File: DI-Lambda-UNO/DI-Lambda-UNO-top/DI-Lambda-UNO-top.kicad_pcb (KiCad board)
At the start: 2 copper layers, 38.2 x 125 mm, 13 parts, among them J1 CONN_02X04, J10 CONN_02X04, J11 CONN_02X04, J12 CONN_02X04, J2 CONN_02X04, J3 CONN_02X04, J4 CONN_02X04, J5 CONN_02X04, J6 CONN_02X04, J7 CONN_02X04, J8 CONN_02X04, J9 CONN_02X04

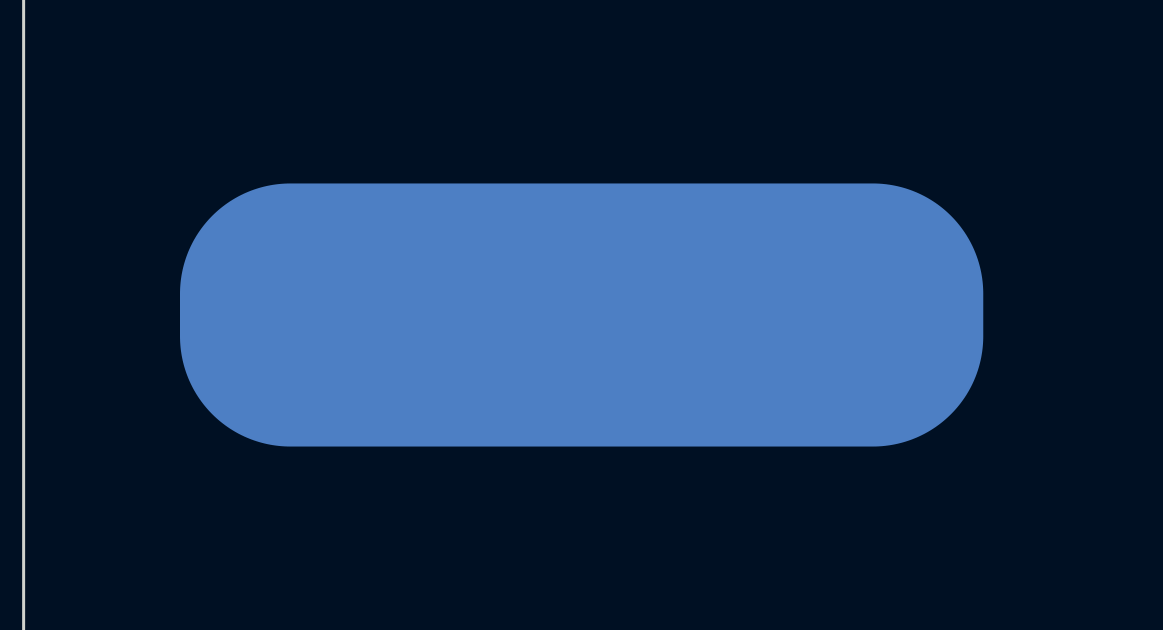
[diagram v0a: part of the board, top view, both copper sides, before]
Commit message: DI-Lambda UNO top panel cleanup
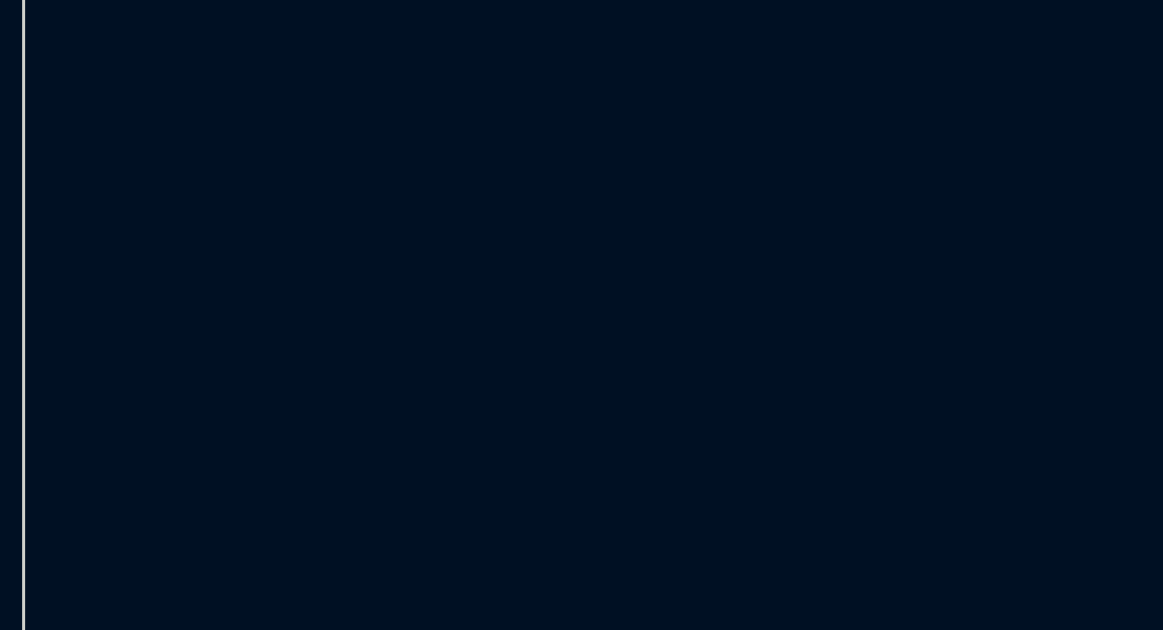
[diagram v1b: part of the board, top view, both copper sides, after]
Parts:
- removed svg2mod: G***, svg2mod:DI-Lambda-UNO-for-Kicad-top-mask

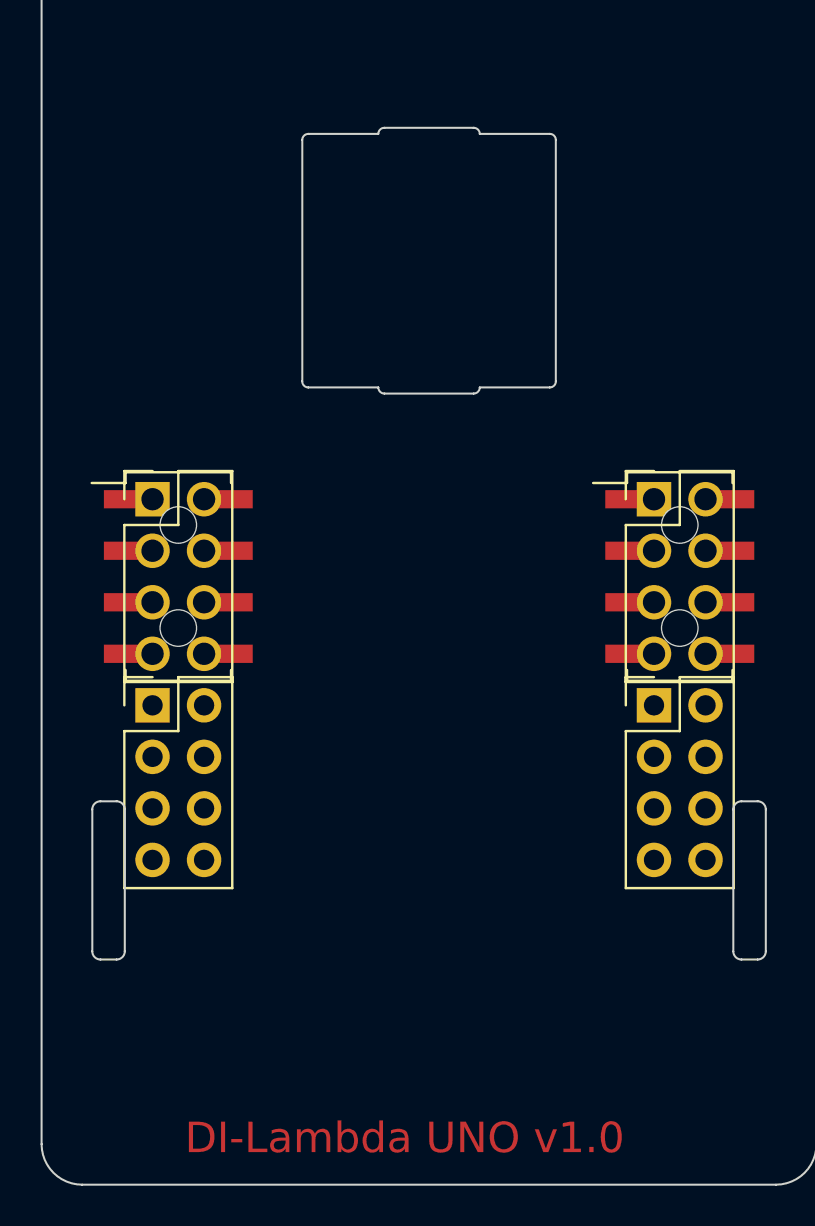
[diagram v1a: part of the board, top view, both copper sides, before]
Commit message: Increase top plate cuvette hole size to 13mm
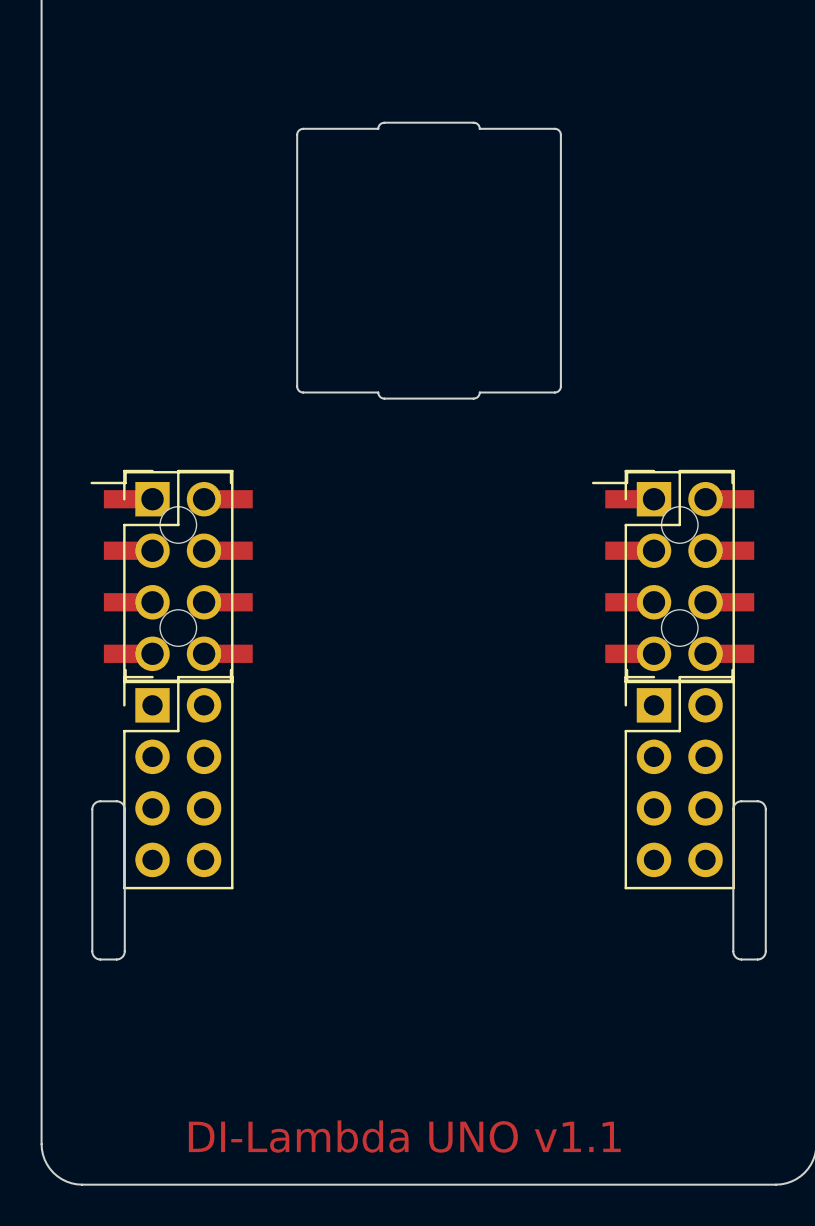
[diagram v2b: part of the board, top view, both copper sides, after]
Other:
- outline, holes or cut-outs redrawn
- board text added: "DI-Lambda UNO v1.1"
- board text removed: "DI-Lambda UNO v1.0"
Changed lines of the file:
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@@
-(kicad_pcb (version 20170123) (host pcbnew "(2017-07-27 revision 3ee2f80)-test1")
+(kicad_pcb (version 20170123) (host pcbnew "(2017-09-07 revision 3b08636)-master")
   (general
     (thickness 1.6)
-    (drawings 89)
+    (drawings 91)
     (tracks 0)
     (zones 0)
@@
       (layerselection 0x000f0_ffffffff)
       (usegerberextensions true)
+      (usegerberattributes true)
+      (usegerberadvancedattributes true)
+      (creategerberjobfile true)
       (excludeedgelayer false)
       (linewidth 0.100000)
@@
     (pad "" np_thru_hole circle (at 0 2.54) (size 1.8 1.8) (drill 1.8) (layers *.Cu *.Mask))
   )
-  (gr_text "DI-Lambda UNO v1.0" (at 147.984 141.464) (layer F.Cu)
+  (dimension 13 (width 0.3) (layer Eco1.User)
+    (gr_text "13.000 mm" (at 149.184 87.364) (layer Eco1.User)
+      (effects (font (size 1.5 1.5) (thickness 0.3)))
+    )
+    (feature1 (pts (xy 155.684 92.014) (xy 155.684 86.014)))
+    (feature2 (pts (xy 142.684 92.014) (xy 142.684 86.014)))
+    (crossbar (pts (xy 142.684 88.714) (xy 155.684 88.714)))
+    (arrow1a (pts (xy 155.684 88.714) (xy 154.557496 89.300421)))
+    (arrow1b (pts (xy 155.684 88.714) (xy 154.557496 88.127579)))
+    (arrow2a (pts (xy 142.684 88.714) (xy 143.810504 89.300421)))
+    (arrow2b (pts (xy 142.684 88.714) (xy 143.810504 88.127579)))
+  )
+  (dimension 13.000096 (width 0.3) (layer Eco1.User)
+    (gr_text "13.000 mm" (at 160.259318 98.19419 270.2203673) (layer Eco1.User)
+      (effects (font (size 1.5 1.5) (thickness 0.3)))
+    )
+    (feature1 (pts (xy 155.134 104.714) (xy 161.634308 104.688998)))
+    (feature2 (pts (xy 155.084 91.714) (xy 161.584308 91.688998)))
+    (crossbar (pts (xy 158.884328 91.699383) (xy 158.934328 104.699383)))
+    (arrow1a (pts (xy 158.934328 104.699383) (xy 158.343579 103.575143)))
+    (arrow1b (pts (xy 158.934328 104.699383) (xy 159.516412 103.570632)))
+    (arrow2a (pts (xy 158.884328 91.699383) (xy 158.302244 92.828134)))
+    (arrow2b (pts (xy 158.884328 91.699383) (xy 159.475077 92.823623)))
+  )
+  (gr_text "DI-Lambda UNO v1.1" (at 147.984 141.464) (layer F.Cu)
     (effects (font (size 1.5 1.5) (thickness 0.3)))
   )
@@
     (arrow2b (pts (xy 127.434 132.264) (xy 128.020421 133.390504)))
   )
-  (gr_arc (start 143.234 92.264) (end 142.934 92.264) (angle 90) (layer Edge.Cuts) (width 0.1))
-  (gr_arc (start 143.234 104.164) (end 143.234 104.464) (angle 90) (layer Edge.Cuts) (width 0.1))
-  (gr_arc (start 146.984 104.464) (end 146.984 104.764) (angle 90) (layer Edge.Cuts) (width 0.1))
-  (gr_arc (start 151.384 104.464) (end 151.684 104.464) (angle 90) (layer Edge.Cuts) (width 0.1))
-  (gr_arc (start 155.134 104.164) (end 155.434 104.164) (angle 90) (layer Edge.Cuts) (width 0.1))
-  (gr_arc (start 155.134 92.264) (end 155.134 91.964) (angle 90) (layer Edge.Cuts) (width 0.1))
-  (gr_arc (start 151.384 91.964) (end 151.384 91.664) (angle 90) (layer Edge.Cuts) (width 0.1))
-  (gr_arc (start 146.984 91.964) (end 146.684 91.964) (angle 90) (layer Edge.Cuts) (width 0.1))
+  (gr_arc (start 142.984 92.014) (end 142.684 92.014) (angle 90) (layer Edge.Cuts) (width 0.1))
+  (gr_arc (start 142.984 104.414) (end 142.984 104.714) (angle 90) (layer Edge.Cuts) (width 0.1))
+  (gr_arc (start 146.984 104.714) (end 146.984 105.014) (angle 90) (layer Edge.Cuts) (width 0.1))
+  (gr_arc (start 151.384 104.714) (end 151.684 104.714) (angle 90) (layer Edge.Cuts) (width 0.1))
+  (gr_arc (start 155.384 104.414) (end 155.684 104.414) (angle 90) (layer Edge.Cuts) (width 0.1))
+  (gr_arc (start 155.384 92.014) (end 155.384 91.714) (angle 90) (layer Edge.Cuts) (width 0.1))
+  (gr_arc (start 151.384 91.714) (end 151.384 91.414) (angle 90) (layer Edge.Cuts) (width 0.1))
+  (gr_arc (start 146.984 91.714) (end 146.684 91.714) (angle 90) (layer Edge.Cuts) (width 0.1))
   (gr_arc (start 165.384 37.264) (end 165.784 37.264) (angle 90) (layer Edge.Cuts) (width 0.1))
   (gr_line (start 164.584 37.664) (end 165.384 37.664) (layer Edge.Cuts) (width 0.1))
@@
   (gr_line (start 132.084 143.764) (end 166.284 143.764) (layer Edge.Cuts) (width 0.1))
   (gr_line (start 166.284 18.764) (end 132.084 18.764) (layer Edge.Cuts) (width 0.1))
-  (gr_line (start 146.684 91.964) (end 143.234 91.964) (layer Edge.Cuts) (width 0.1))
-  (gr_line (start 142.934 92.264) (end 142.934 104.164) (layer Edge.Cuts) (width 0.1))
-  (gr_line (start 155.134 91.964) (end 151.684 91.964) (layer Edge.Cuts) (width 0.1))
-  (gr_line (start 146.984 91.664) (end 151.384 91.664) (layer Edge.Cuts) (width 0.1))
+  (gr_line (start 146.684 91.714) (end 142.984 91.714) (layer Edge.Cuts) (width 0.1))
+  (gr_line (start 142.684 92.014) (end 142.684 104.414) (layer Edge.Cuts) (width 0.1))
+  (gr_line (start 155.384 91.714) (end 151.684 91.714) (layer Edge.Cuts) (width 0.1))
+  (gr_line (start 146.984 91.414) (end 151.384 91.414) (layer Edge.Cuts) (width 0.1))
   (gr_line (start 164.184 78.564) (end 164.184 83.964) (layer Edge.Cuts) (width 0.1))
-  (gr_line (start 155.134 104.464) (end 151.684 104.464) (layer Edge.Cuts) (width 0.1))
+  (gr_line (start 155.384 104.714) (end 151.684 104.714) (layer Edge.Cuts) (width 0.1))
   (gr_line (start 130.084 141.764) (end 130.084 20.764) (layer Edge.Cuts) (width 0.1))
   (gr_line (start 164.184 37.264) (end 164.184 30.264) (layer Edge.Cuts) (width 0.1))
-  (gr_line (start 143.234 104.464) (end 146.684 104.464) (layer Edge.Cuts) (width 0.1))
+  (gr_line (start 142.984 104.714) (end 146.684 104.714) (layer Edge.Cuts) (width 0.1))
   (gr_line (start 165.784 125.264) (end 165.784 132.264) (layer Edge.Cuts) (width 0.1))
   (gr_line (start 164.184 132.264) (end 164.184 125.264) (layer Edge.Cuts) (width 0.1))
-  (gr_line (start 155.434 104.164) (end 155.434 92.264) (layer Edge.Cuts) (width 0.1))
+  (gr_line (start 155.684 104.414) (end 155.684 92.014) (layer Edge.Cuts) (width 0.1))
   (gr_line (start 132.584 37.264) (end 132.584 30.264) (layer Edge.Cuts) (width 0.1))
   (gr_line (start 132.584 132.264) (end 132.584 125.264) (layer Edge.Cuts) (width 0.1))
@@
   (gr_line (start 134.184 84.764) (end 132.584 84.764) (layer Edge.Cuts) (width 0.1))
   (gr_line (start 134.184 30.264) (end 134.184 37.264) (layer Edge.Cuts) (width 0.1))
-  (gr_line (start 151.384 104.764) (end 146.984 104.764) (layer Edge.Cuts) (width 0.1))
+  (gr_line (start 151.384 105.014) (end 146.984 105.014) (layer Edge.Cuts) (width 0.1))
   (gr_line (start 165.784 30.264) (end 165.784 37.264) (layer Edge.Cuts) (width 0.1))
   (gr_line (start 165.784 78.564) (end 165.784 83.964) (layer Edge.Cuts) (width 0.1))
@@
     (polygon
       (pts
-        (xy 143.434 92.264) (xy 154.934 92.264) (xy 154.934 104.014) (xy 143.184 104.014)
+        (xy 142.884 91.864) (xy 155.434 91.914) (xy 155.434 104.514) (xy 142.984 104.464)
       )
     )
@@
     (polygon
       (pts
-        (xy 143.387863 92.264) (xy 154.887863 92.264) (xy 154.887863 104.014) (xy 143.137863 104.014)
+        (xy 142.884 91.864) (xy 155.434 91.914) (xy 155.384 104.514) (xy 142.934 104.464)
       )
     )
